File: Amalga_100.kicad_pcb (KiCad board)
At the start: 6 copper layers, 268 x 155 mm, 231 parts, among them IC1 ADM3052, IC3 INA240A1, IC4 INA240A1, IC5 INA240A1, P1 USB_B, P10 IN-, P2 Interface, P3 IN+, P4 IN-, P5 MOTOR3, P6 MOTOR2, P7 MOTOR1, P8 SWD, P9 CONN_6-HSWR-V2-rescue, Q1 IRFP4668PBF, Q10 IRFP4668PBF, Q11 IRFP4668PBF, Q12 IRFP4668PBF, Q13 BC846B, Q14 BC856B, Q15 BC846B, Q16 BC856B, Q2 IRFP4668PBF, Q3 IRFP4668PBF, Q4 IRFP4668PBF, Q5 IRFP4668PBF, Q6 IRFP4668PBF, Q7 IRFP4668PBF, Q8 IRFP4668PBF, Q9 IRFP4668PBF, SW1 SW_DIP_x02, U1 STM32F40X_LQFP64, U10 AD8664ARZ, U2 B1215S-2W, U3 JW5052C, U4 JW5052C, U5 ADUM3160, U6 AD2S1200YSTZ, U7 IRS2186, U8 IRS2186, U9 IRS2186, Y1 8MHz, Y2 8.912 MHZ

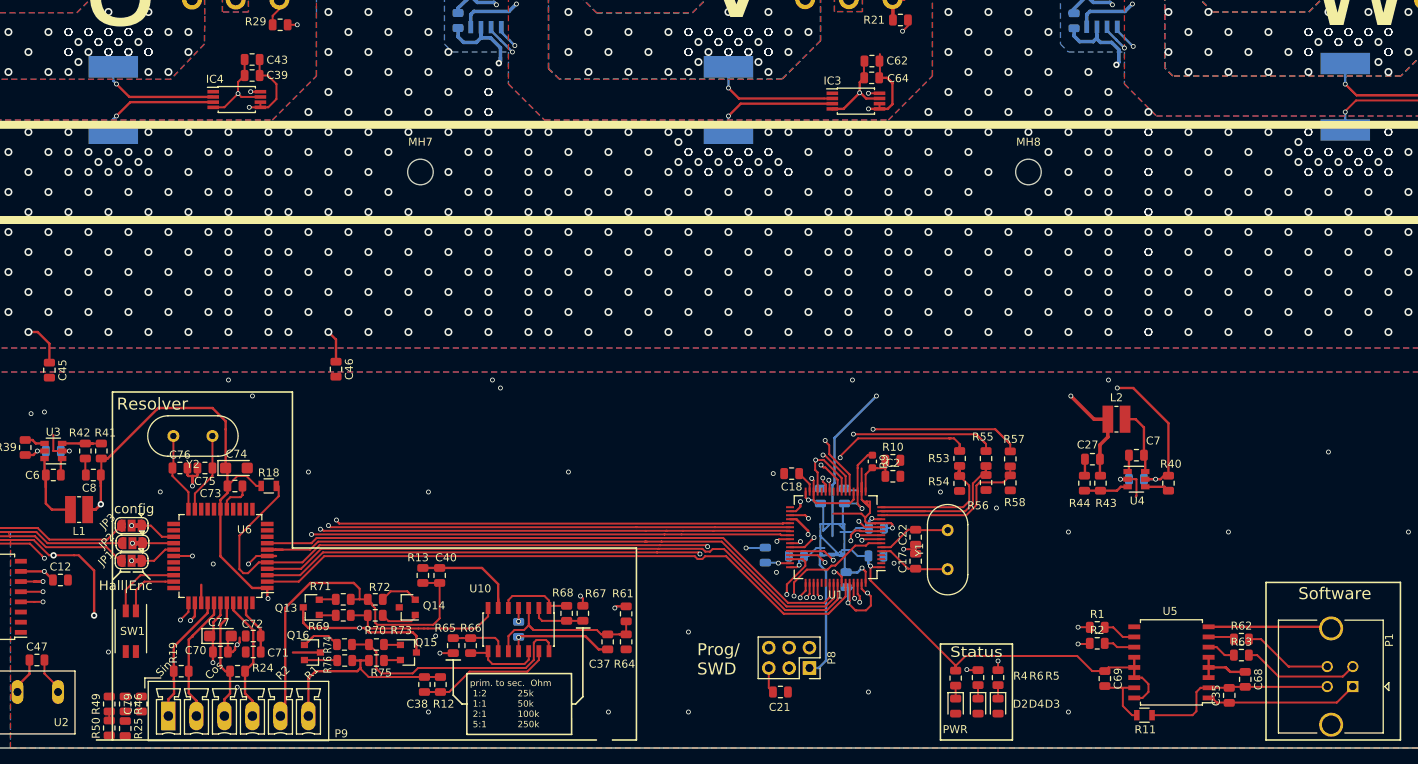
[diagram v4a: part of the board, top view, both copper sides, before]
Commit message: added dc-bias for adc sin/cos resolver
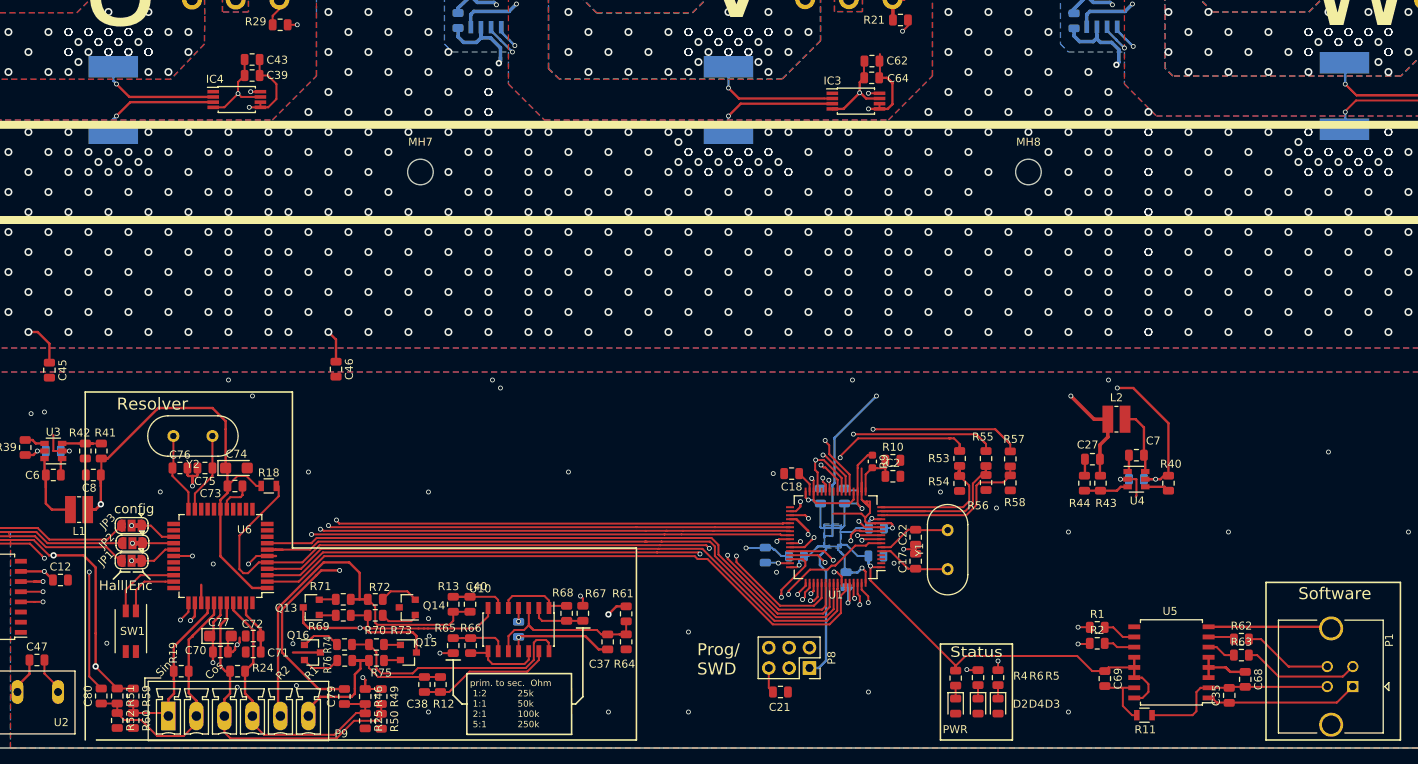
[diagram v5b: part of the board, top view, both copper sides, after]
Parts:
- added C80: 10nF, Capacitor_SMD:C_0805_2012Metric, F.Cu at (75.0, 161.0)
- added R51: 50k, Resistor_SMD:R_0805_2012Metric, F.Cu at (77.0, 161.0)
- added R52: 50k, Resistor_SMD:R_0805_2012Metric, F.Cu at (77.0, 164.1)
- added R59: 50k, Resistor_SMD:R_0805_2012Metric, F.Cu at (79.0, 161.0)
- added R60: 50k, Resistor_SMD:R_0805_2012Metric, F.Cu at (79.0, 164.1)
- R25, R46, R49, R50: value 68k -> 50k
- moved R49 34.0 mm to (110.0, 161.1), turned to 270 degrees
- moved R50 34.0 mm to (110.0, 164.2), turned to 270 degrees
- moved R25 30.0 mm to (108.0, 164.1)
- moved R46 30.0 mm to (108.0, 161.1)
- moved C79 25.4 mm to (105.4, 161.1)
- moved C40 5.24 mm to (121.1, 149.5)
- moved R13 5.24 mm to (119.0, 149.5)
- moved R48 0.14 mm to (230.4, 86.0)
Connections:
- C79 pad 2: /Resolver/µC1_RES -> COS_analog_RES
- R49 pad 1: /Resolver/CosLO(S6) -> +5V
- R49 pad 2: +5V -> /Resolver/CosLO(S6)
- R50 pad 1: GND -> /Resolver/CosLO(S6)
- R50 pad 2: /Resolver/CosLO(S6) -> GND
- U1 pad 2: /Resolver/*RDvel -> Net-(U1-Pad2)
- U1 pad 26: /MCU/SIN_IN_RES -> SIN_analog_RES
- U1 pad 27: /MCU/COS_IN_RES -> COS_analog_RES
- U1 pad 53: /Resolver/*CS -> /Resolver/*RDvel
- U1 pad 54: Net-(U1-Pad54) -> /Resolver/*CS
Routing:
- net SIN_analog_RES: track 0.00 -> 118.1 mm, vias 0 -> 2
- net COS_analog_RES: track 0.00 -> 97.2 mm, vias 0 -> 2
- net /Resolver/*CS: track 4.11 -> 77.3 mm, vias 0 -> 2
- net /MCU/SIN_IN_RES: track 72.6 -> 0.00 mm, vias 2 -> 0
- net /Resolver/*RDvel: track 21.1 -> 93.3 mm, vias 0 -> 2
- net /MCU/COS_IN_RES: track 72.2 -> 0.00 mm, vias 2 -> 0
- net /Resolver/CosLO(S6): track 19.4 -> 43.1 mm
- net +5V: track 210.2 -> 230.7 mm
- net /Resolver/Cos(S2): track 19.7 -> 39.6 mm
- net /Resolver/SinLO(S3): track 16.0 -> 31.8 mm
- net Net-(C40-Pad2): track 15.5 -> 6.79 mm
- net /Resolver/Sin(S1): track 16.2 -> 21.9 mm
- net +3V3: track 607.8 -> 602.4 mm
- net /Resolver/R2: track 47.7 -> 52.1 mm
- net /Resolver/Buffer Circuit R2D/*EXC: track 38.2 -> 42.5 mm
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
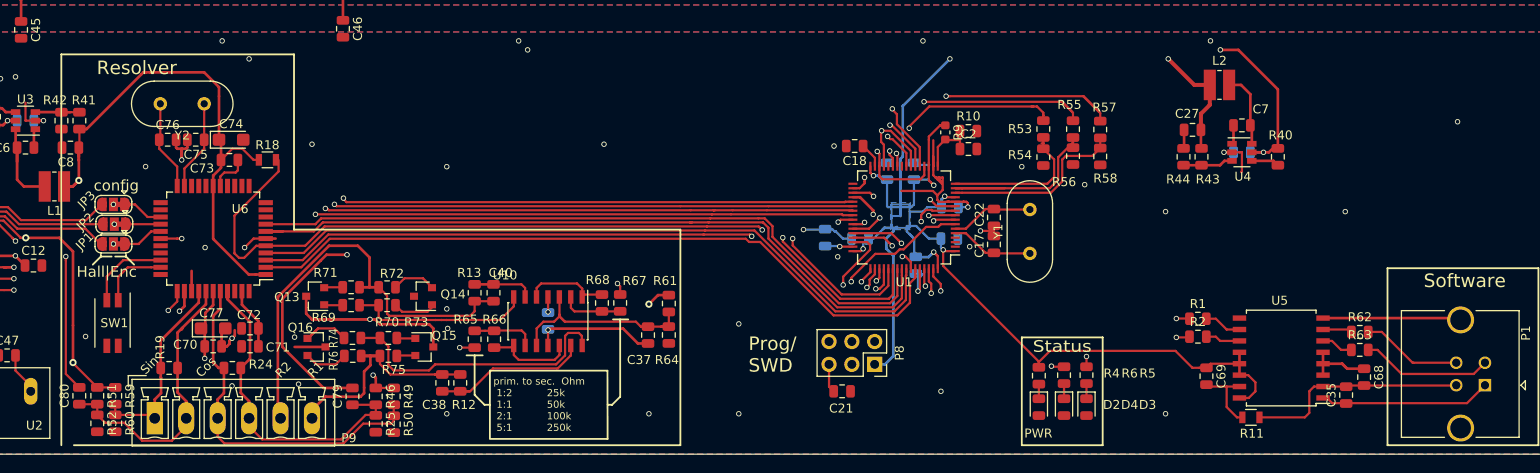
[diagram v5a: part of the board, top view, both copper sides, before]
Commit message: activated pulldown res on usb-Isolator IC
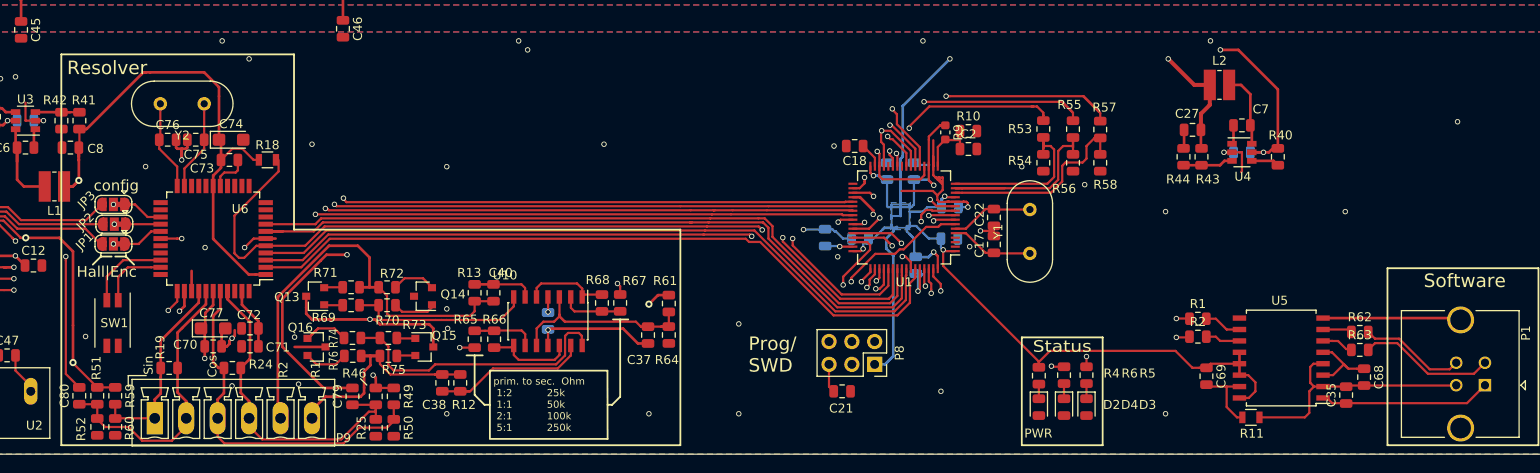
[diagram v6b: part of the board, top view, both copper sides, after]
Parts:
- moved R56 0.75 mm to (185.6, 135.1)
- moved R58 0.70 mm to (188.6, 135.1)
- moved R54 0.63 mm to (182.3, 135.1)
- moved R25 0.45 mm to (108.0, 164.6)
- moved R50 0.40 mm to (110.0, 164.6)
- moved R52 0.40 mm to (77.0, 164.5)
- moved R60 0.40 mm to (79.0, 164.5)
- renumbered R48 to R45
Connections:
- IC1 pad 10: Net-(IC1-Pad10) -> (no net)
- P8 pad 6: Net-(P8-Pad6) -> (no net)
- U1 pad 2: Net-(U1-Pad2) -> (no net)
- U1 pad 25: Net-(U1-Pad25) -> (no net)
- U1 pad 28: Net-(U1-Pad28) -> (no net)
- U1 pad 3: Net-(U1-Pad3) -> (no net)
- U1 pad 33: Net-(U1-Pad33) -> (no net)
- U1 pad 4: Net-(U1-Pad4) -> (no net)
- U5 pad 4: Net-(C68-Pad1) -> /USB-Isolator/GND1
- U6 pad 10: Net-(U6-Pad10) -> (no net)
- U6 pad 11: Net-(U6-Pad11) -> (no net)
- U6 pad 12: Net-(U6-Pad12) -> (no net)
- U6 pad 13: Net-(U6-Pad13) -> (no net)
- U6 pad 14: Net-(U6-Pad14) -> (no net)
- U6 pad 15: Net-(U6-Pad15) -> (no net)
- U6 pad 18: Net-(U6-Pad18) -> (no net)
- U6 pad 19: Net-(U6-Pad19) -> (no net)
- U6 pad 20: Net-(U6-Pad20) -> (no net)
- U6 pad 24: Net-(U6-Pad24) -> (no net)
- U6 pad 29: Net-(U6-Pad29) -> (no net)
- U6 pad 30: Net-(U6-Pad30) -> (no net)
- U6 pad 33: Net-(U6-Pad33) -> (no net)
- U6 pad 44: Net-(U6-Pad44) -> (no net)
- U6 pad 9: Net-(U6-Pad9) -> (no net)
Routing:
- net /USB-Isolator/GND1: track 55.0 -> 58.9 mm
- net /MCU/SENS1: track 16.4 -> 18.9 mm
- net /Filters/TEMP_IN: track 158.3 -> 160.5 mm
- net /MCU/SENS2: track 23.3 -> 25.4 mm
- net /MCU/SENS3: track 20.7 -> 22.3 mm
- net /Resolver/Cos(S2): track 39.6 -> 41.0 mm
- net Net-(C68-Pad1): track 7.90 -> 8.67 mm
- net /USB-Isolator/UD+: track 11.2 -> 11.8 mm
- net /USB-Isolator/UD-: track 14.6 -> 15.2 mm
- net Net-(R63-Pad1): track 4.18 -> 3.59 mm
